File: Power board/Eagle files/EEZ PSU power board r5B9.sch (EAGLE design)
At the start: 272 parts, among them IC1 LTC3864EMSE#PBF, IC10 REF5025AIDG4, IC11 DAC8552IDGKTG4, IC12 ADG465SOT-23, IC13 TS5A9411DCKT, IC14 ADS1120IPWR, IC15 LP339D, IC2 MC79L05, IC3 MC78L05, IC4 LM5574MTX/NOPB, IC5 LP2951SO8, IC6 TL072D, IC7 TL072D, IC8 OP27GSZ, IC9 MCP23S08-E/SO, Q1 SUD19P06-60, Q10 MMBT5401, Q11 MMBT5401, Q12 MMBT5551, Q13 MMBT5551, Q14 BSS84P, Q15 2N7002, Q16 MMBT5551, Q17 MMBT5401, Q18 MMBT5551, Q19 MMBT5551, Q2 MMBT5401, Q3 2N7002, Q4 IRFP250N, Q5 BC857C, Q6 BC846C, Q7 BCP56-16.115, Q8 IRFR5410, Q9 BCP56-16.115, X1 39303035, X2 282836-2, X3 SSW-113-02-T-D-RA

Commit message: C39 marked as n.c.
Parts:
- C39: value 2u2 -> n.c.
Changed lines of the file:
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@@
 <part name="D10" library="EEZ_Lib1" deviceset="SCHOTTKY" device="SOD123" value="DFLS1100-7"/>
 <part name="C31" library="rcl" deviceset="C-EU" device="C1206" value="1u/100V"/>
-<part name="C39" library="rcl" deviceset="C-EU" device="C0805" value="2u2">
+<part name="C39" library="rcl" deviceset="C-EU" device="C0805" value="n.c.">
 <variant name="Farnell" value="2320829"/>
 <variant name="TME" value="CL21B225KAFNNNG "/>

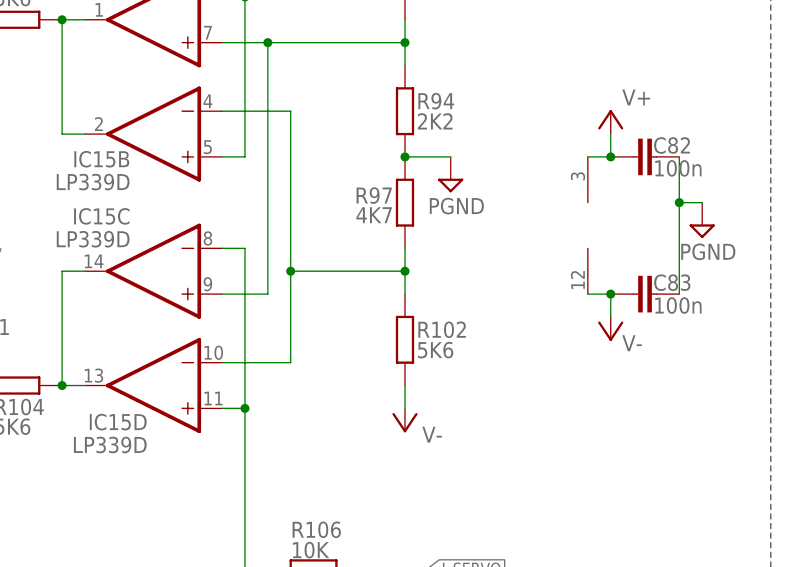
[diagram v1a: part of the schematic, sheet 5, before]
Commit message: R97 and R102 values swapped
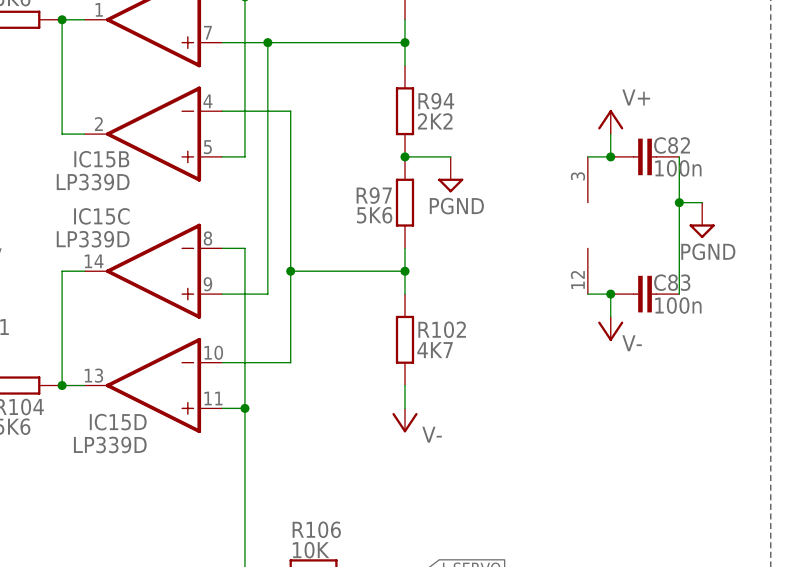
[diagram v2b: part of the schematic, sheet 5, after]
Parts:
- R102: value 5K6 -> 4K7
- R97: value 4K7 -> 5K6
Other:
- note added: "-2.72V"
- note removed: "-2.27V"
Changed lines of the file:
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@@
 <part name="C73" library="rcl" deviceset="C-EU" device="C0603" value="100n"/>
 <part name="FRAME5" library="frames" deviceset="DINA4_L" device=""/>
-<part name="R102" library="rcl" deviceset="R-EU_" device="R0805" value="5K6"/>
+<part name="R102" library="rcl" deviceset="R-EU_" device="R0805" value="4K7"/>
 <part name="R94" library="rcl" deviceset="R-EU_" device="R0805" value="2K2"/>
 <part name="R92" library="rcl" deviceset="R-EU_" device="R0805" value="5K6"/>
@@
 <part name="SUPPLY4" library="supply2" deviceset="GND" device="" value="PGND"/>
 <part name="SUPPLY22" library="supply2" deviceset="GND" device="" value="PGND"/>
-<part name="R97" library="rcl" deviceset="R-EU_" device="R0805" value="4K7"/>
+<part name="R97" library="rcl" deviceset="R-EU_" device="R0805" value="5K6"/>
 <part name="SUPPLY1" library="supply2" deviceset="GND" device="" value="PGND"/>
 <part name="SUPPLY2" library="supply2" deviceset="-9V" device=""/>
@@
 <polygon width="0.1524" layer="101">
 </polygon>
-<text x="88.265" y="118.745" size="1.27" layer="100" rot="MR180">-2.27V</text>
+<text x="88.265" y="118.745" size="1.27" layer="100" rot="MR180">-2.72V</text>
 <text x="2.54" y="7.62" size="1.778" layer="94">Licensed under the TAPR Open Hardware License (www.tapr.org/OHL)</text>
 <text x="2.54" y="2.54" size="1.778" layer="94">Repository: https://github.com/eez-open</text>
